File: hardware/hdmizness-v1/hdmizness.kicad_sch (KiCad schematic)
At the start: 65 parts, among them J1 HDMI_A_PCB, J2 USB_A_PCB, SW1 SW_Push, U1 F1C100s, U2 TDA19988, U3 W25Q128JVPIQ, U4 EA3058, Y1 24M

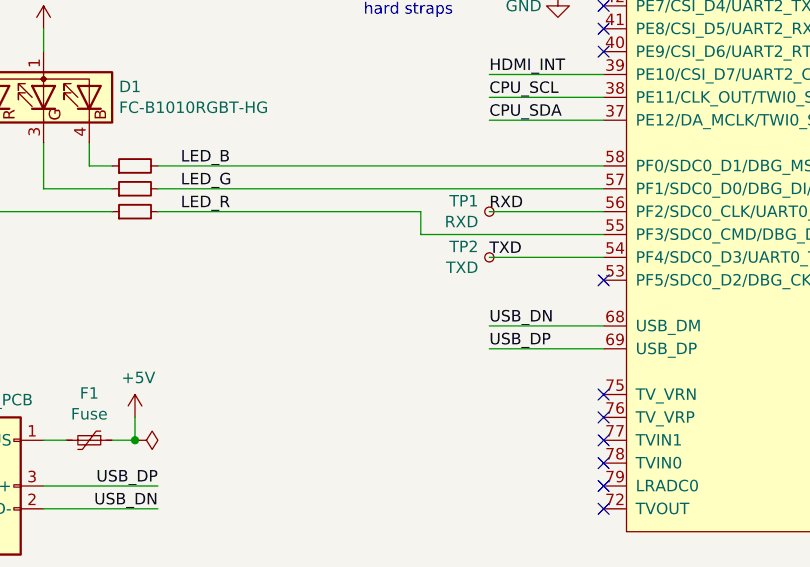
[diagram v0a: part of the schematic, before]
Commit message: hardware: don't put soldermask in front of pcb connectors
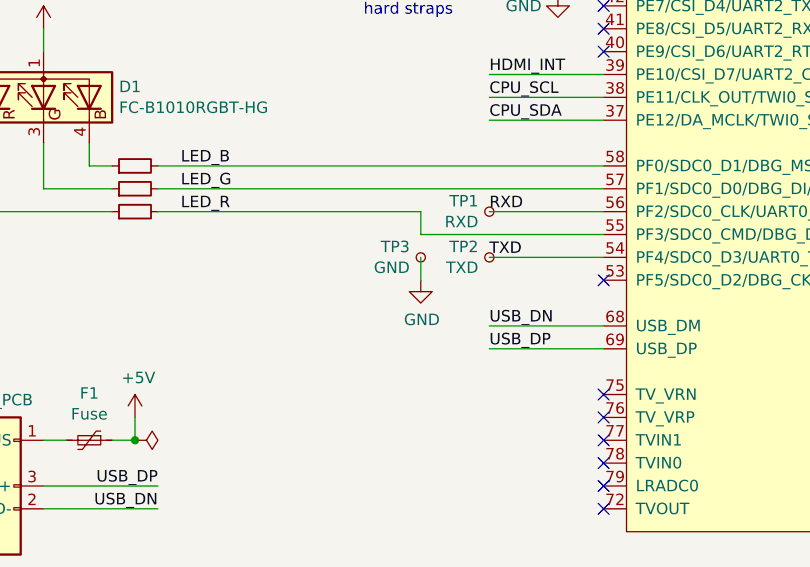
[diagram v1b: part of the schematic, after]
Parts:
- added TP3: GND, TestPoint:TestPoint_Pad_1.0x1.0mm, symbol Connector:TestPoint_Small
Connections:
- net GND: now also TP3.1
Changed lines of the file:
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@@
 	(wire
 		(pts
+			(xy 82.55 140.97) (xy 82.55 143.51)
+		)
+		(stroke
+			(width 0)
+			(type default)
+		)
+	)
+	(wire
+		(pts
 			(xy 316.23 173.99) (xy 316.23 176.53)
 		)
@@
 					(unit 1)
 				)
+			)
+		)
+	)
+	(symbol
+		(lib_id "power:GND")
+		(at 82.55 143.51 0)
+		(unit 1)
+		(exclude_from_sim no)
+		(in_bom yes)
+		(on_board yes)
+		(dnp no)
+		(property "Reference" "#PWR050"
+			(at 82.55 149.86 0)
+			(effects
+				(font
+					(size 1.27 1.27)
+				)
+				(hide yes)
+			)
+		)
+		(property "Value" "GND"
+			(at 82.677 147.9042 0)
+			(effects
+				(font
+					(size 1.27 1.27)
+				)
+			)
+		)
+		(property "Footprint" ""
+			(at 82.55 143.51 0)
+			(effects
+				(font
+					(size 1.27 1.27)
+				)
+				(hide yes)
+			)
+		)
+		(property "Datasheet" ""
+			(at 82.55 143.51 0)
+			(effects
+				(font
+					(size 1.27 1.27)
+				)
+				(hide yes)
+			)
+		)
+		(property "Description" ""
+			(at 82.55 143.51 0)
+			(effects
+				(font
+					(size 1.27 1.27)
+				)
+			)
+		)
+		(pin "1"
+		)
+		(instances
+			(project "hdmizness"
+				(path "/09c0df14-58b4-4c4a-bb4e-79b7696a1706"
+					(reference "#PWR050")
+					(unit 1)
+				)
+			)
+		)
+	)
+	(symbol
+		(lib_id "Connector:TestPoint_Small")
+		(at 82.55 140.97 0)
+		(mirror x)
+		(unit 1)
+		(exclude_from_sim no)
+		(in_bom yes)
+		(on_board yes)
+		(dnp no)
+		(property "Reference" "TP3"
+			(at 81.3308 139.8016 0)
+			(effects
+				(font
+					(size 1.27 1.27)
+				)
+				(justify right)
+			)
+		)
+		(property "Value" "GND"
+			(at 81.3308 142.113 0)
+			(effects
+				(font
+					(size 1.27 1.27)
+				)
+				(justify right)
+			)
+		)
+		(property "Footprint" "TestPoint:TestPoint_Pad_1.0x1.0mm"
+			(at 87.63 140.97 0)
+			(effects
+				(font
+					(size 1.27 1.27)
+				)
+				(hide yes)
+			)
+		)
+		(property "Datasheet" "~"
+			(at 87.63 140.97 0)
+			(effects
+				(font
+					(size 1.27 1.27)
+				)
+				(hide yes)
+			)
+		)
+		(property "Description" ""
+			(at 82.55 140.97 0)
+			(effects
+				(font
+					(size 1.27 1.27)
+				)
+			)
+		)
+		(pin "1"
+		)
+		(instances
+			(project "hdmizness"
+				(path "/09c0df14-58b4-4c4a-bb4e-79b7696a1706"
+					(reference "TP3")
+					(unit 1)
+				)

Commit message: hardware: update bom with chips now on LCSC
F1C100s, SiI9022A and TDA19988 are now available on LCSC. Set the proper
fields to show them on the BoM.
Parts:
- D1: LCSC P/N (none) -> C158099; MFR P/N (none) -> FC-B1010RGBT-HG
- U1: LCSC P/N (none) -> C1511928; MFR P/N (none) -> F1C100S
- U2: LCSC P/N (none) -> C1523269; MFR P/N (none) -> TDA19988BHN
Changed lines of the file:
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@@
 			)
 		)
+		(property "LCSC P/N" "C1523269"
+			(at 257.81 67.31 0)
+			(effects
+				(font
+					(size 1.27 1.27)
+				)
+				(hide yes)
+			)
+		)
+		(property "MFR P/N" "TDA19988BHN"
+			(at 257.81 67.31 0)
+			(effects
+				(font
+					(size 1.27 1.27)
+				)
+				(hide yes)
+			)
+		)
 		(pin "32"
 		)
@@
 			)
 		)
+		(property "LCSC P/N" "C1511928"
+			(at 105.41 67.31 0)
+			(effects
+				(font
+					(size 1.27 1.27)
+				)
+				(hide yes)
+			)
+		)
+		(property "MFR P/N" "F1C100S"
+			(at 105.41 67.31 0)
+			(effects
+				(font
+					(size 1.27 1.27)
+				)
+				(hide yes)
+			)
+		)
 		(pin "40"
 		)
@@
 			)
 		)
+		(property "LCSC P/N" "C1511928"
+			(at 271.78 203.2 0)
+			(effects
+				(font
+					(size 1.27 1.27)
+				)
+				(hide yes)
+			)
+		)
+		(property "MFR P/N" "F1C100S"
+			(at 271.78 203.2 0)
+			(effects
+				(font
+					(size 1.27 1.27)
+				)
+				(hide yes)
+			)
+		)
 		(pin "66"
 		)
@@
 			)
 		)
+		(property "LCSC P/N" "C158099"
+			(at 40.64 123.19 0)
+			(effects
+				(font
+					(size 1.27 1.27)
+				)
+				(hide yes)
+			)
+		)
+		(property "MFR P/N" "FC-B1010RGBT-HG"
+			(at 40.64 123.19 0)
+			(effects
+				(font
+					(size 1.27 1.27)
+				)
+				(hide yes)
+			)
+		)
